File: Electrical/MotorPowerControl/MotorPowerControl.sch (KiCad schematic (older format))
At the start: 10 parts, among them J1 Conn_01x03, J2 178.6164.0002, J3 Conn_01x03, J4 178.6164.0002, J5 178.6164.0002, J6 178.6164.0002

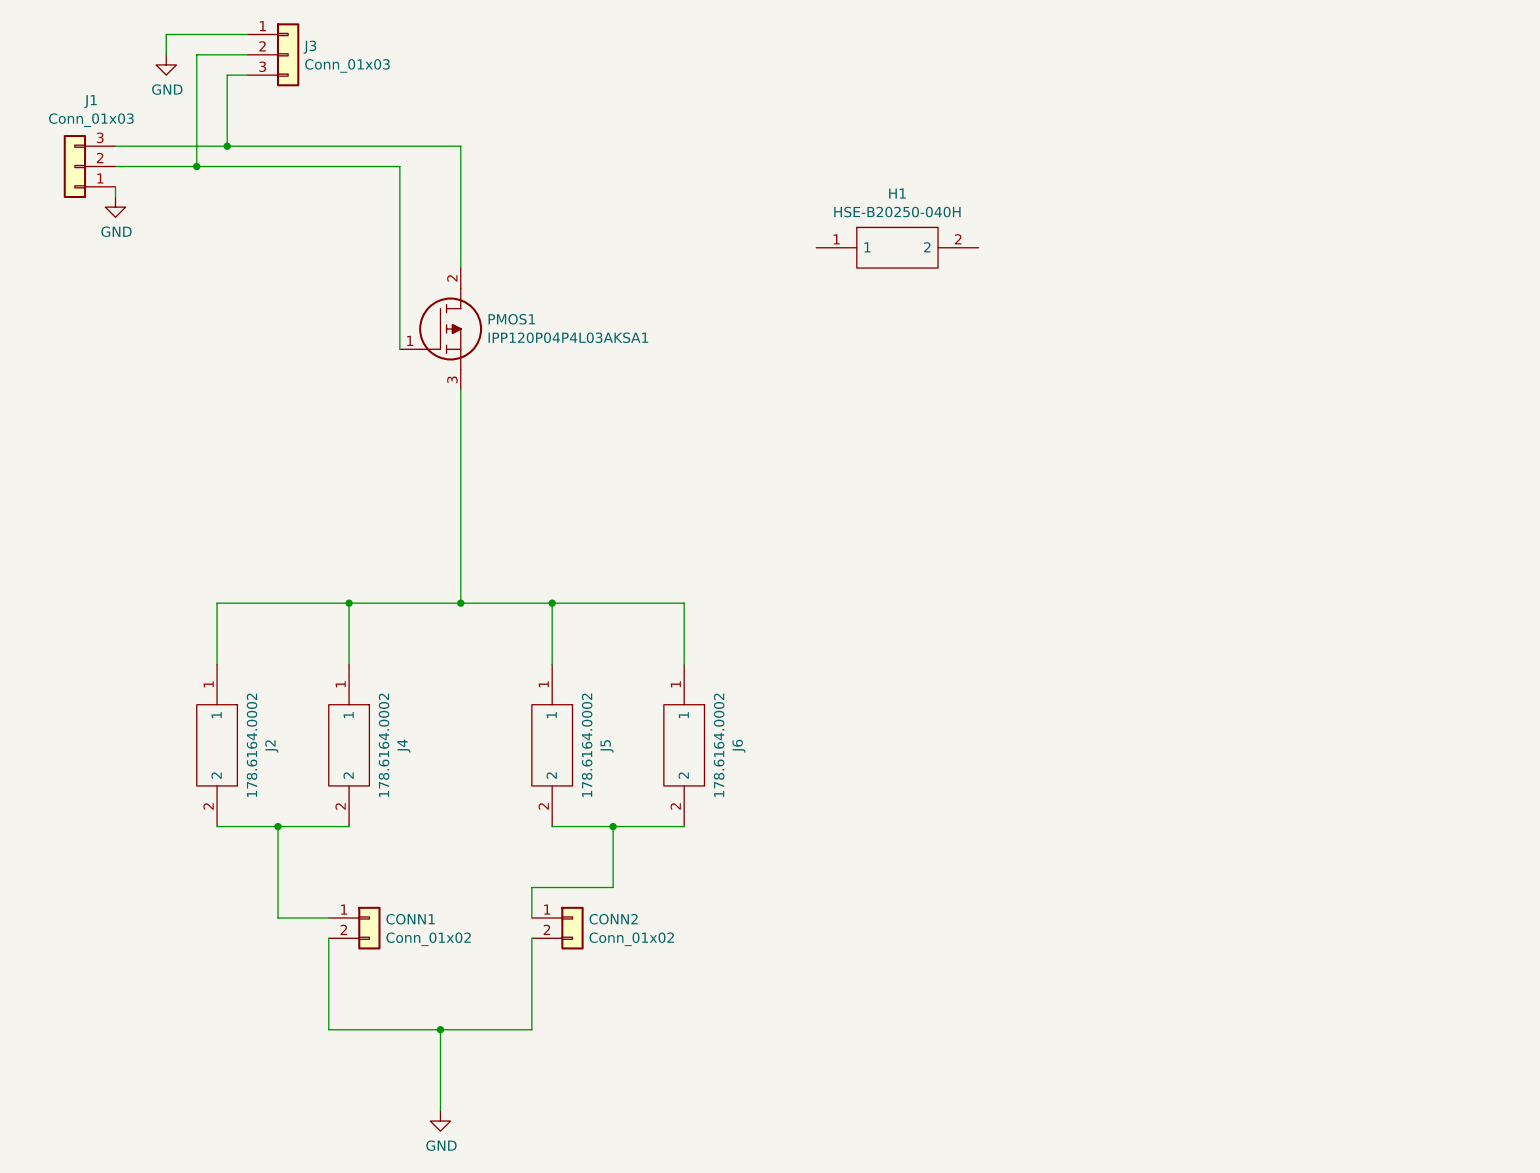
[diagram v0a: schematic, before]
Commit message: Verified Peripheral and Motor power controllers
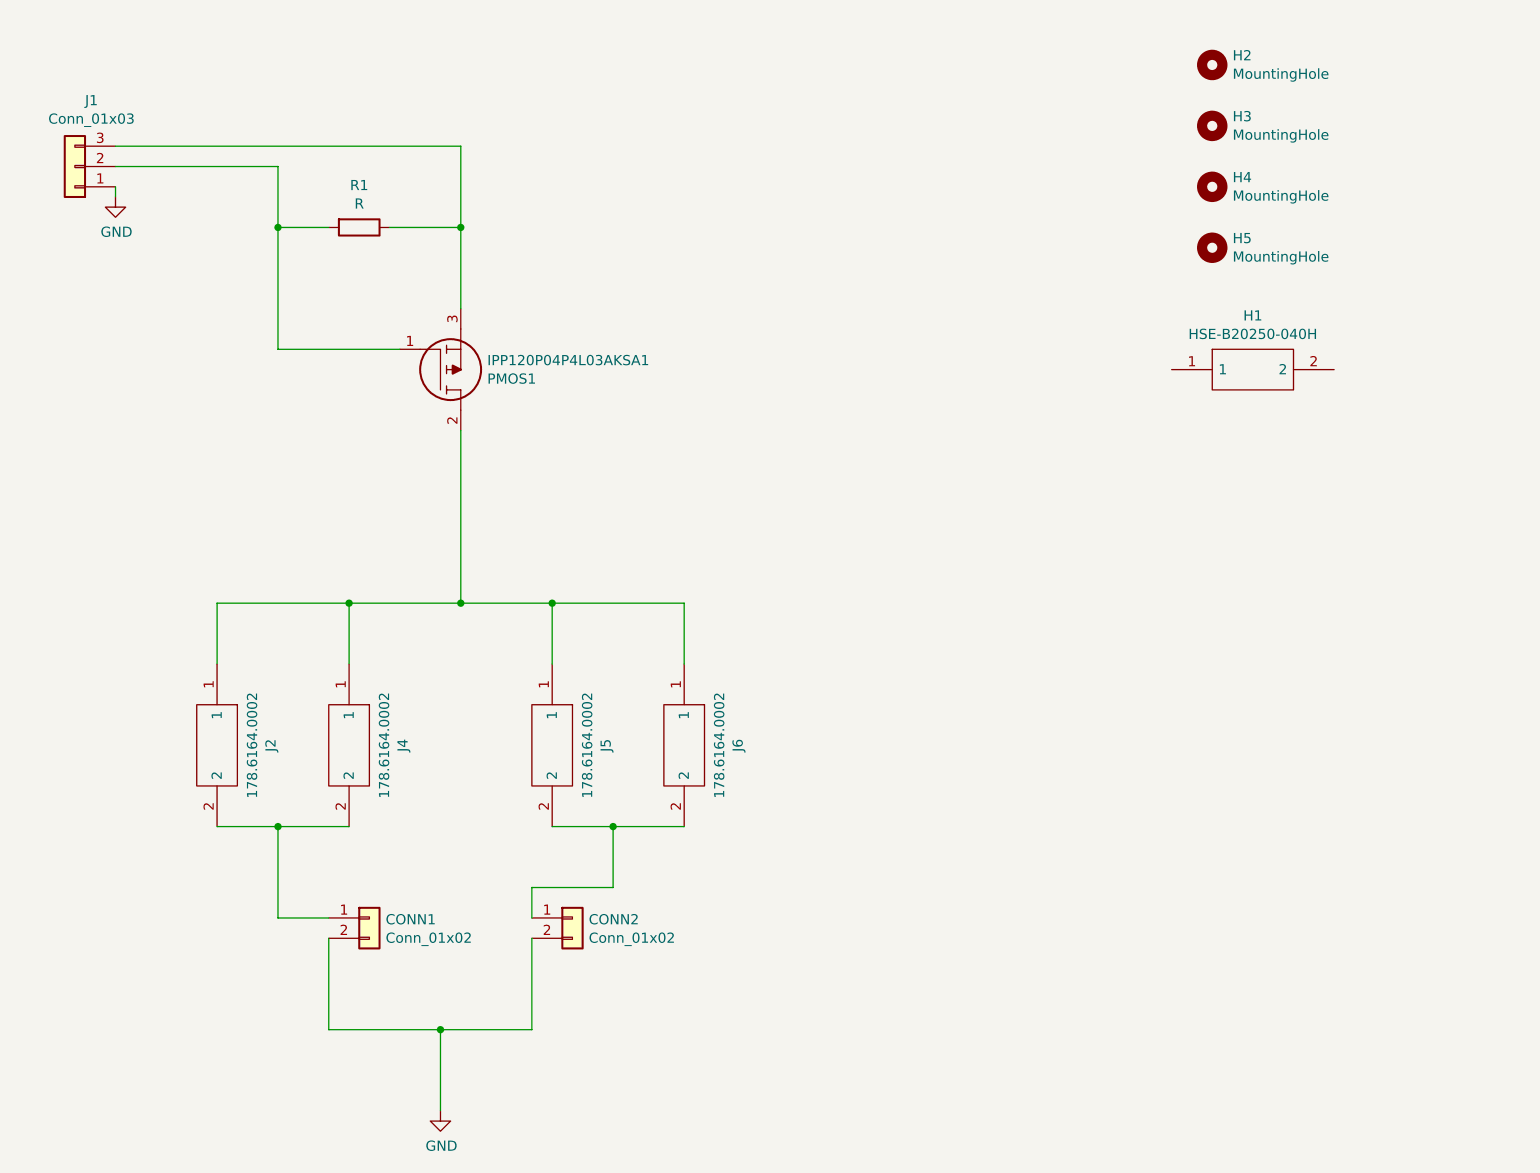
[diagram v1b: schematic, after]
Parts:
- removed J3: Conn_01x03, Connector_Wire:SolderWirePad_1x03_P7.62mm_Drill2.5mm, symbol Connector_Generic:Conn_01x03
- added H2, H3, H4, H5: MountingHole, MountingHole:MountingHole_3.2mm_M3, symbol Mechanical:MountingHole
- added R1: R, Resistor_THT:R_Axial_DIN0204_L3.6mm_D1.6mm_P7.62mm_Horizontal, symbol Device:R
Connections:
- net at J1.2 (Pin_2), PMOS1.1: now also R1.2
- net at J1.3 (Pin_3): now also PMOS1.3, R1.1; no longer PMOS1.2
- net at J2.1, J4.1, J5.1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: now also PMOS1.2; no longer PMOS1.3
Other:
- moved on the sheet: H1, PMOS1
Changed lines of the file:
@@
 EESchema Schematic File Version 4
+LIBS:MotorPowerControl-cache
 EELAYER 30 0
 EELAYER END
@@
 F 9 "IPP120P04P4L03AKSA1" H 5500 1600 50  0001 L CNN "Manufacturer_Part_Number"
 	1    5050 2350
-	1    0    0    -1
-$EndComp
-Wire Wire Line
-	5350 3600 5350 2550
+	1    0    0    1
+$EndComp
 $Comp
 L LibraryLoader:178.6164.0002 J6
@@
 $EndComp
 Wire Wire Line
-	5350 3600 4800 3600
-Wire Wire Line
 	4150 3600 4150 3900
 Wire Wire Line
@@
 Wire Wire Line
 	5800 3900 5800 3600
-Wire Wire Line
-	5800 3600 5350 3600
-Connection ~ 5350 3600
 Wire Wire Line
 	6450 3900 6450 3600
@@
 	-1   0    0    1
 $EndComp
-$Comp
-L Connector_Generic:Conn_01x03 J3
-U 1 1 5D956F16
-P 4500 900
-F 0 "J3" H 4580 942 50  0000 L CNN
-F 1 "Conn_01x03" H 4580 851 50  0000 L CNN
-F 2 "Connector_Wire:SolderWirePad_1x03_P7.62mm_Drill2.5mm" H 4500 900 50  0001 C CNN
-F 3 "~" H 4500 900 50  0001 C CNN
-	1    4500 900
-	1    0    0    -1
-$EndComp
-Wire Wire Line
-	3650 1350 4200 1350
-Wire Wire Line
-	5350 1350 5350 1950
-Wire Wire Line
-	3650 1450 4050 1450
-Wire Wire Line
-	5050 1450 5050 2350
+Wire Wire Line
+	5350 1350 5350 1750
+Wire Wire Line
+	4450 1450 4450 1750
 Wire Wire Line
 	3650 1600 3650 1550
@@
 	1    0    0    -1
 $EndComp
-Wire Wire Line
-	4300 1000 4200 1000
-Wire Wire Line
-	4200 1000 4200 1350
-Connection ~ 4200 1350
-Wire Wire Line
-	4200 1350 5350 1350
-Wire Wire Line
-	4300 900  4050 900
-Wire Wire Line
-	4050 900  4050 1450
-Connection ~ 4050 1450
-Wire Wire Line
-	4050 1450 5050 1450
-$Comp
-L power:GND #PWR02
-U 1 1 5D95E094
-P 3900 900
-F 0 "#PWR02" H 3900 650 50  0001 C CNN
-F 1 "GND" H 3905 727 50  0000 C CNN
-F 2 "" H 3900 900 50  0001 C CNN
-F 3 "" H 3900 900 50  0001 C CNN
-	1    3900 900
-	1    0    0    -1
-$EndComp
-Wire Wire Line
-	4300 800  3900 800
-Wire Wire Line
-	3900 800  3900 900
 $Comp
 L LibraryLoader:HSE-B20250-040H H1
 U 1 1 5D9636D1
-P 7100 1850
-F 0 "H1" H 7500 2115 50  0000 C CNN
-F 1 "HSE-B20250-040H" H 7500 2024 50  0000 C CNN
-F 2 "LibraryLoader:HSEB20250040H" H 7750 1950 50  0001 L CNN
-F 3 "https://componentsearchengine.com/Datasheets/1/HSE-B20250-040H.pdf" H 7750 1850 50  0001 L CNN
-F 4 "Heat Sinks 25x35x12.5mm w/pin extrusion TO-220" H 7750 1750 50  0001 L CNN "Description"
-F 5 "25" H 7750 1650 50  0001 L CNN "Height"
-F 6 "490-HSE-B20250-040H" H 7750 1550 50  0001 L CNN "Mouser Part Number"
-F 7 "https://www.mouser.com/Search/Refine.aspx?Keyword=490-HSE-B20250-040H" H 7750 1450 50  0001 L CNN "Mouser Price/Stock"
-F 8 "CUI" H 7750 1350 50  0001 L CNN "Manufacturer_Name"
-F 9 "HSE-B20250-040H" H 7750 1250 50  0001 L CNN "Manufacturer_Part_Number"
-	1    7100 1850
-	1    0    0    -1
-$EndComp
+P 8850 2450
+F 0 "H1" H 9250 2715 50  0000 C CNN
+F 1 "HSE-B20250-040H" H 9250 2624 50  0000 C CNN
+F 2 "LibraryLoader:HSEB20250040H" H 9500 2550 50  0001 L CNN
+F 3 "https://componentsearchengine.com/Datasheets/1/HSE-B20250-040H.pdf" H 9500 2450 50  0001 L CNN
+F 4 "Heat Sinks 25x35x12.5mm w/pin extrusion TO-220" H 9500 2350 50  0001 L CNN "Description"
+F 5 "25" H 9500 2250 50  0001 L CNN "Height"
+F 6 "490-HSE-B20250-040H" H 9500 2150 50  0001 L CNN "Mouser Part Number"
+F 7 "https://www.mouser.com/Search/Refine.aspx?Keyword=490-HSE-B20250-040H" H 9500 2050 50  0001 L CNN "Mouser Price/Stock"
+F 8 "CUI" H 9500 1950 50  0001 L CNN "Manufacturer_Name"
+F 9 "HSE-B20250-040H" H 9500 1850 50  0001 L CNN "Manufacturer_Part_Number"
+	1    8850 2450
+	1    0    0    -1
+$EndComp
+$Comp
+L Mechanical:MountingHole H3
+U 1 1 5D9BF700
+P 9050 1250
+F 0 "H3" H 9150 1296 50  0000 L CNN
+F 1 "MountingHole" H 9150 1205 50  0000 L CNN
+F 2 "MountingHole:MountingHole_3.2mm_M3" H 9050 1250 50  0001 C CNN
+F 3 "~" H 9050 1250 50  0001 C CNN
+	1    9050 1250
+	1    0    0    -1
+$EndComp
+$Comp
+L Mechanical:MountingHole H2
+U 1 1 5D9C0051
+P 9050 950
+F 0 "H2" H 9150 996 50  0000 L CNN
+F 1 "MountingHole" H 9150 905 50  0000 L CNN
+F 2 "MountingHole:MountingHole_3.2mm_M3" H 9050 950 50  0001 C CNN
+F 3 "~" H 9050 950 50  0001 C CNN
+	1    9050 950
+	1    0    0    -1
+$EndComp
+$Comp
+L Mechanical:MountingHole H4
+U 1 1 5D9C0B50
+P 9050 1550
+F 0 "H4" H 9150 1596 50  0000 L CNN
+F 1 "MountingHole" H 9150 1505 50  0000 L CNN
+F 2 "MountingHole:MountingHole_3.2mm_M3" H 9050 1550 50  0001 C CNN
+F 3 "~" H 9050 1550 50  0001 C CNN
+	1    9050 1550
+	1    0    0    -1
+$EndComp
+$Comp
+L Mechanical:MountingHole H5
+U 1 1 5D9C15C6
+P 9050 1850
+F 0 "H5" H 9150 1896 50  0000 L CNN
+F 1 "MountingHole" H 9150 1805 50  0000 L CNN
+F 2 "MountingHole:MountingHole_3.2mm_M3" H 9050 1850 50  0001 C CNN
+F 3 "~" H 9050 1850 50  0001 C CNN
+	1    9050 1850
+	1    0    0    -1
+$EndComp
+Wire Wire Line
+	3650 1350 5350 1350
+Wire Wire Line
+	3650 1450 4450 1450
+$Comp
+L Device:R R1
+U 1 1 5D9CA0C3
+P 4850 1750
+F 0 "R1" V 4643 1750 50  0000 C CNN
+F 1 "R" V 4734 1750 50  0000 C CNN
+F 2 "Resistor_THT:R_Axial_DIN0204_L3.6mm_D1.6mm_P7.62mm_Horizontal" V 4780 1750 50  0001 C CNN
+F 3 "~" H 4850 1750 50  0001 C CNN
+	1    4850 1750
+	0    1    1    0
+$EndComp
+Wire Wire Line
+	4700 1750 4450 1750
+Connection ~ 4450 1750
+Wire Wire Line
+	4450 1750 4450 2350
+Wire Wire Line
+	5000 1750 5350 1750
+Wire Wire Line
+	5050 2350 4450 2350
+Wire Wire Line
+	4800 3600 5350 3600
+Wire Wire Line
+	5350 2150 5350 1750
+Connection ~ 5350 1750
+Wire Wire Line
+	5350 2750 5350 3600
+Connection ~ 5350 3600
+Wire Wire Line
+	5350 3600 5800 3600
 $EndSCHEMATC

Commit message: Adds PDFs to show schematics and comments the motor power module some
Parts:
- H1: symbol LibraryLoader:HSE-B20250-040H -> MotorPowerControl-rescue:HSE-B20250-040H-LibraryLoader
- J2, J4, J5, J6: symbol LibraryLoader:178.6164.0002 -> MotorPowerControl-rescue:178.6164.0002-LibraryLoader
- PMOS1: symbol LibraryLoader:IPP120P04P4L03AKSA1 -> MotorPowerControl-rescue:IPP120P04P4L03AKSA1-LibraryLoader
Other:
- note added: "Pull-up resistor to cut power if\nenable is disconnected"
- note added: "This is a heatsink for cooling the PMOS"
- note added: "VCC\nENB\nGND"
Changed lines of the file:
@@
 EESchema Schematic File Version 4
-LIBS:MotorPowerControl-cache
 EELAYER 30 0
 EELAYER END
@@
 $EndDescr
 $Comp
-L LibraryLoader:IPP120P04P4L03AKSA1 PMOS1
+L MotorPowerControl-rescue:IPP120P04P4L03AKSA1-LibraryLoader PMOS1
 U 1 1 5D9583CA
 P 5050 2350
@@
 $EndComp
 $Comp
-L LibraryLoader:178.6164.0002 J6
+L MotorPowerControl-rescue:178.6164.0002-LibraryLoader J6
 U 1 1 5D9583D7
 P 6450 3900
@@
 $EndComp
 $Comp
-L LibraryLoader:178.6164.0002 J5
+L MotorPowerControl-rescue:178.6164.0002-LibraryLoader J5
 U 1 1 5D9583E3
 P 5800 3900
@@
 $EndComp
 $Comp
-L LibraryLoader:178.6164.0002 J4
+L MotorPowerControl-rescue:178.6164.0002-LibraryLoader J4
 U 1 1 5D9583EF
 P 4800 3900
@@
 $EndComp
 $Comp
-L LibraryLoader:178.6164.0002 J2
+L MotorPowerControl-rescue:178.6164.0002-LibraryLoader J2
 U 1 1 5D9583FB
 P 4150 3900
@@
 $EndComp
 $Comp
-L LibraryLoader:HSE-B20250-040H H1
+L MotorPowerControl-rescue:HSE-B20250-040H-LibraryLoader H1
 U 1 1 5D9636D1
 P 8850 2450
@@
 Wire Wire Line
 	5350 3600 5800 3600
+Text Notes 8710 2720 0    50   ~ 0
+This is a heatsink for cooling the PMOS
+Text Notes 5440 1800 0    50   ~ 0
+Pull-up resistor to cut power if\nenable is disconnected
+Text Notes 3160 1570 0    50   ~ 0
+VCC\nENB\nGND
 $EndSCHEMATC
